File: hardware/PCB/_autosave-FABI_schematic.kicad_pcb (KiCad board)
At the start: 2 copper layers, 79 x 55 mm, 47 parts, among them J1 Cliff_68125, J10 Conn_01x03_Male, J11 dispaly_connector_91601-304LF, J11_disp1 Conn_01x04_Female, J2 Cliff_68125, J3 Cliff_68125, J4 Cliff_68125, J5 Cliff_68125, J6 Cliff_68125, J7 Cliff_68125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

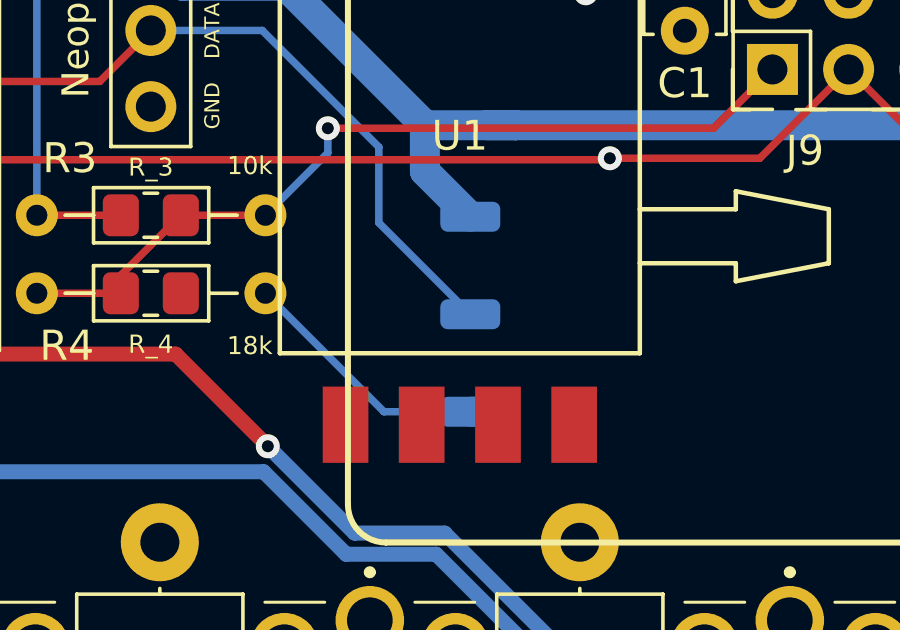
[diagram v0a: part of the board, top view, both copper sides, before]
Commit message: updated PCB edges, to mount PCB with M3 screws, minor changes to size and some element positions, SMD NeoPixel pads updated
Signed-off-by: fussthalerandreas <fussthaler.andreas1997@gmail.com>
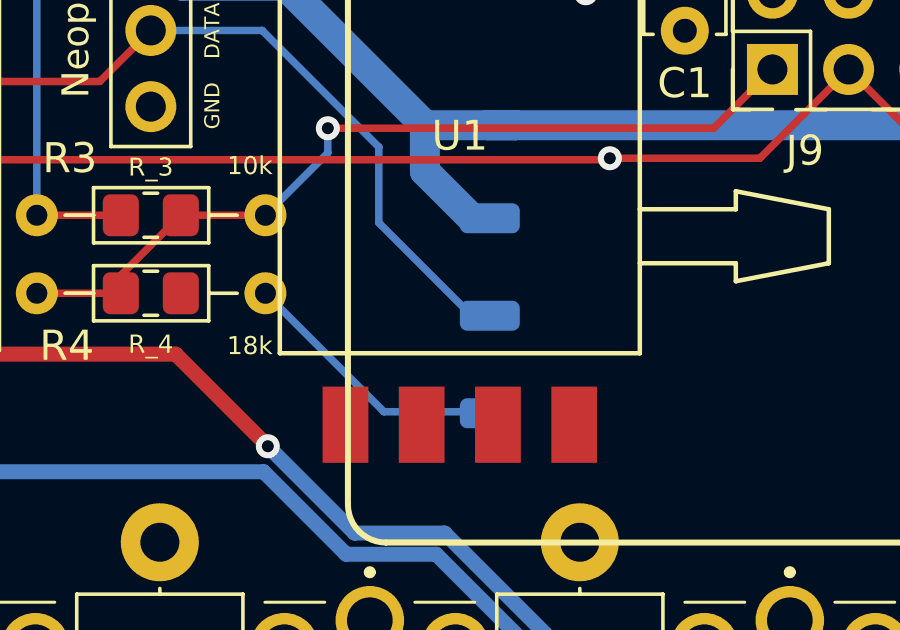
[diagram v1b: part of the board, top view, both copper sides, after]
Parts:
- removed DATA, GND, VDD: SolderWirePad_1x01_SMD_1x2mm, Connector_Wire:SolderWirePad_1x01_SMD_1x2mm
- added J11_GND1: Conn_01x01_Male, Connector_Wire:SolderWirePad_1x01_SMD_1x2mm, B.Cu at (133.2, 119.3)
- added J11_VDD1: Conn_01x01_Male, Connector_Wire:SolderWirePad_1x01_SMD_1x2mm, B.Cu at (133.2, 112.8)
- added J11_data1: Conn_01x01_Male, Connector_Wire:SolderWirePad_1x01_SMD_1x2mm, B.Cu at (133.2, 116.1)
